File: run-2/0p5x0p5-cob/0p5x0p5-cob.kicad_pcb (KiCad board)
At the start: 2 copper layers, 14 x 16 mm, 7 parts

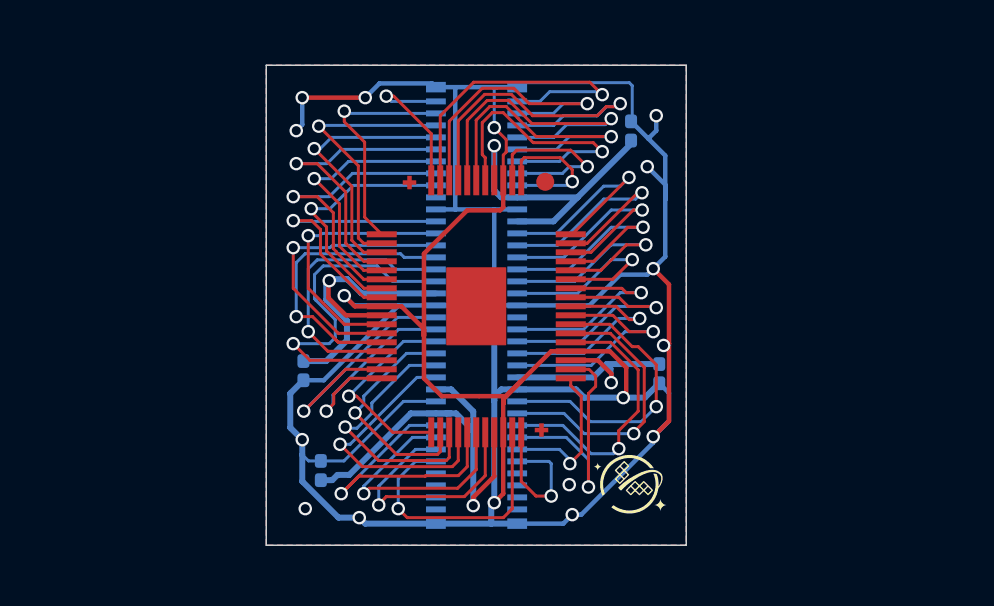
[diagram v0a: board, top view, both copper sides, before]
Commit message: updating libs for 76 pin
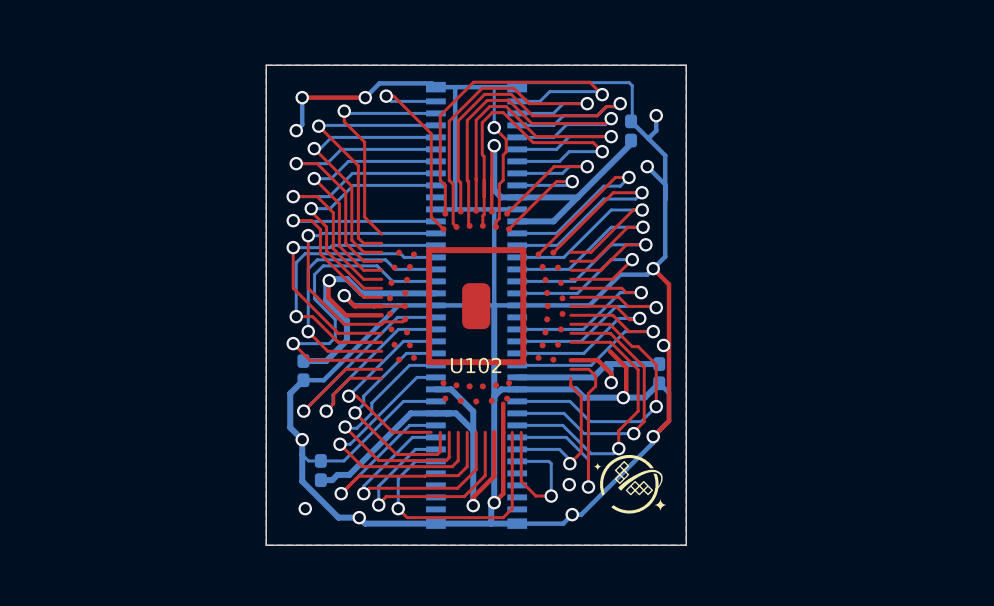
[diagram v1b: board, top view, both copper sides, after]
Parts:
- U102: footprint WaferSpace:waferspace_p5xp5_padring -> WaferSpace:waferspace_p5xp5_padring_staggered
- turned U102 to 180 degrees
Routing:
- net GND: track 121.2 -> 104.0 mm
- net /bidir_0: track 9.61 -> 11.7 mm
- net VDD_IO_3: track 10.5 -> 12.6 mm
- net /bidir_6: track 5.30 -> 7.10 mm
- net /bidir_4: track 9.71 -> 11.4 mm
- net /bidir_2: track 10.9 -> 12.4 mm
- net /bidir_37: track 7.18 -> 8.57 mm
- net /bidir_5: track 11.2 -> 12.4 mm
- net /bidir_3: track 11.9 -> 13.0 mm
- net /bidir_1: track 10.4 -> 11.5 mm
- net /bidir_15: track 8.99 -> 9.84 mm
- net /bidir_36: track 7.96 -> 8.81 mm

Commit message: finished init routing front only
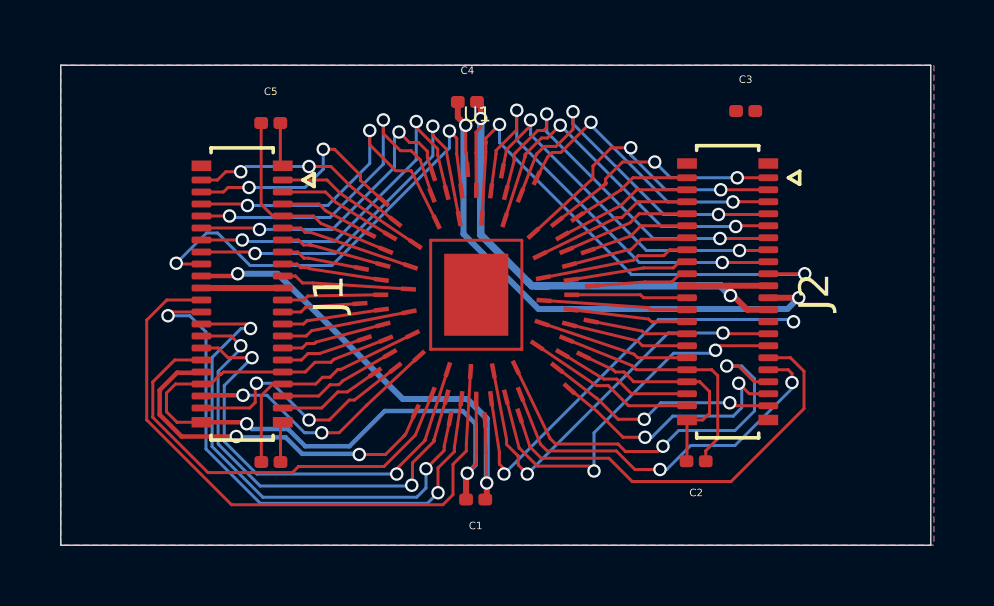
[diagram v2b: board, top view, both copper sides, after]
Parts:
- removed C101, C102, C104, C108: C_Small, Capacitor_SMD:C_0201_0603Metric
- removed G***: LOGO, Symbol:waferspace_pin1_silk
- removed U101: ~, WaferSpace:CONN-SMD_70P-P0.40_HCTL_HC-PBB40C-70DP-0.4V-02
- removed U102: ~, WaferSpace:waferspace_p5xp5_padring_staggered
- added C1: 1uF, Capacitor_SMD:C_0201_0603Metric, F.Cu at (127.0, 98.2)
- added C2: 1uF, Capacitor_SMD:C_0201_0603Metric, F.Cu at (134.3, 96.9)
- added C3: 1uF, Capacitor_SMD:C_0201_0603Metric, F.Cu at (136.0, 85.2)
- added C4: 1uF, Capacitor_SMD:C_0201_0603Metric, F.Cu at (126.7, 84.9)
- added C5: 1uF, Capacitor_SMD:C_0201_0603Metric, F.Cu at (120.2, 85.6)
- added C6: 1uF, Capacitor_SMD:C_0201_0603Metric, F.Cu at (120.2, 96.9)
- added J1: Conn_02x20_Odd_Even_MountingPin, Connector_Hirose_DF40:Hirose_DF40C-40DP-0.4V_2x20-1MP_P0.4mm, F.Cu at (119.2, 91.3)
- added J2: Conn_02x20_Odd_Even_MountingPin, Connector_Hirose_DF40:Hirose_DF40C-40DP-0.4V_2x20-1MP_P0.4mm, F.Cu at (135.4, 91.3)
- added U1: ~, WaferSpace:0p5x0p5_76, F.Cu at (127.0, 91.4)
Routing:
- net GND: track 104.0 -> 69.9 mm, vias 17 -> 4
- net VDD_IO_4: track 0.00 -> 19.4 mm, vias 0 -> 2
- net /bidir_38: track 0.00 -> 13.4 mm, vias 0 -> 2
- net /bidir_39: track 0.00 -> 12.3 mm, vias 0 -> 2
- net /bidir_41: track 0.00 -> 11.6 mm, vias 0 -> 2
- net /bidir_42: track 0.00 -> 11.4 mm, vias 0 -> 2
- net /bidir_19: track 11.4 -> 0.00 mm, vias 1 -> 0
- net /bidir_17: track 11.4 -> 0.00 mm, vias 1 -> 0
- net /bidir_26: track 10.7 -> 0.00 mm, vias 1 -> 0
- net /bidir_40: track 0.00 -> 10.5 mm, vias 0 -> 2
- net Net-(J2-Pin_3): track 0.00 -> 9.93 mm, vias 0 -> 2
- net /bidir_27: track 9.93 -> 0.00 mm, vias 1 -> 0
- net /bidir_4: track 11.4 -> 21.2 mm, vias 1 -> 0
- net /bidir_12: track 9.88 -> 0.00 mm, vias 1 -> 0
- net /bidir_15: track 9.84 -> 0.00 mm, vias 1 -> 0
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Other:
- board size 14 x 16 mm -> 29 x 16 mm
- board text removed: "Allocated Space For Passives"

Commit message: designed v1 of 76 pin package
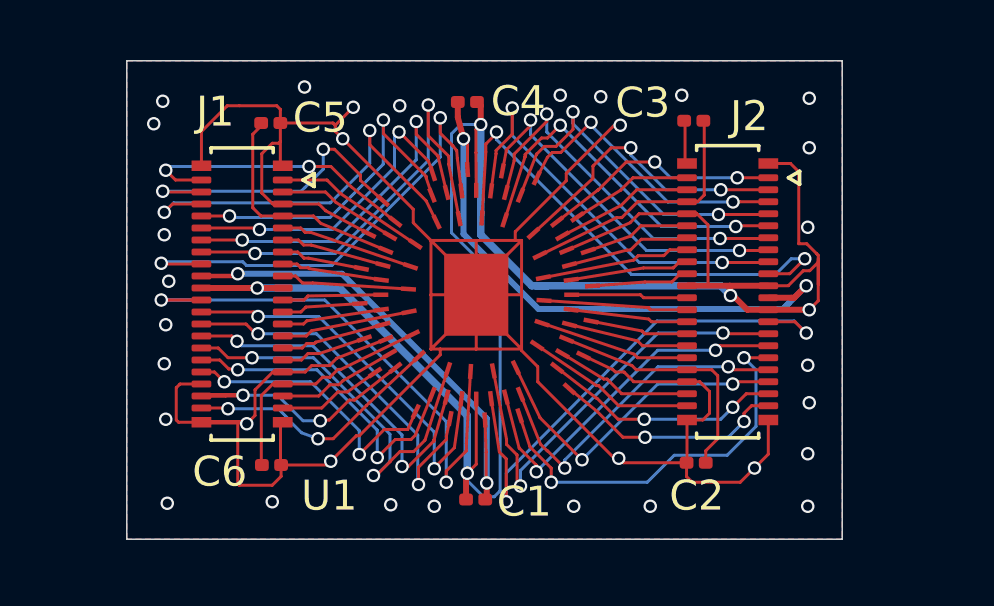
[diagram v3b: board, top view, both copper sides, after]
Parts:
- added CAT_1: pusheen_graphics, WaferSpace:pusheen_back, B.Cu at (118.7, 85.8)
- moved C3 1.76 mm to (134.2, 85.6), turned to 180 degrees
- moved C6 0.10 mm to (120.2, 97.0)
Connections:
- U1 pad 16: Net-(J2-Pin_37) -> Net-(J2-Pin_39)
- U1 pad 17: Net-(J2-Pin_39) -> Net-(J2-Pin_37)
- U1 pad 75: Net-(J1-Pin_40) -> Net-(J1-Pin_38)
- U1 pad 76: Net-(J1-Pin_38) -> Net-(J1-Pin_40)
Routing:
- net GND: track 69.9 -> 172.2 mm, vias 4 -> 37
- net /bidir_3: track 18.6 -> 13.3 mm
- net /bidir_2: track 16.9 -> 13.0 mm
- net /rst_n: track 14.6 -> 10.8 mm, vias 0 -> 2
- net /bidir_5: track 14.5 -> 18.2 mm
- net /bidir_1: track 15.4 -> 12.1 mm
- net VDD_IO_3: track 5.41 -> 8.53 mm
- net /clk: track 12.3 -> 9.49 mm
- net /bidir_10: track 14.0 -> 11.1 mm
- net /bidir_4: track 21.2 -> 18.5 mm, vias 0 -> 2
- net Net-(J1-Pin_4): track 7.90 -> 10.4 mm
- net /bidir_42: track 11.4 -> 13.9 mm
- net Net-(J1-Pin_2): track 7.34 -> 9.72 mm
- net /bidir_9: track 13.0 -> 11.3 mm
- net /bidir_38: track 13.4 -> 14.8 mm
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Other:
- board size 29 x 16 mm -> 23.8 x 16 mm
- board text added: "Heretical Affogato v1.0"
- board text removed: "70 PIN MEZZANINE 56 PIN PADRING VERSION: 0p5x0p5"
- board text removed: "wafer.space GF180MCU Run 2"
